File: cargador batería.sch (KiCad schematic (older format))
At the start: 4 parts, among them U2 MCP73831-2-OT

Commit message: Esquema corregido, PCB terminada
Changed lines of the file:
@@
 EESchema Schematic File Version 4
+LIBS:tpFinal-cache
 EELAYER 26 0
 EELAYER END
@@
 encoding utf-8
 Sheet 2 6
-Title ""
-Date ""
-Rev ""
-Comp ""
+Title "Sistema de comunicación en tiempo real por mensajes de voz
+"
+Date "2018-10-16"
+Rev "1.0"
+Comp "Marcelo Pistarelli"
 Comment1 ""
 Comment2 ""
@@
 Wire Wire Line
 	4750 3600 4900 3600
-Wire Wire Line
-	5300 3800 5300 3950
-Wire Wire Line
-	4750 3950 5300 3950
-Connection ~ 5300 3950
 $Comp
 L Device:C C?
@@
 	1    0    0    -1
 $EndComp
-Wire Wire Line
-	4300 3950 4750 3950
-Connection ~ 4750 3950
 $Comp
 L Device:C C?
@@
 $EndComp
 Wire Wire Line
-	4300 3650 4300 3950
-Wire Wire Line
 	4300 3350 4300 3200
 Wire Wire Line
@@
 Wire Wire Line
 	6400 3400 6400 3450
-Wire Wire Line
-	6400 3750 6400 3950
-Wire Wire Line
-	6400 3950 5300 3950
 Text HLabel 6800 3400 2    50   Output ~ 0
 BAT+
@@
 	6800 3400 6400 3400
 Connection ~ 6400 3400
-Text HLabel 6800 3950 2    50   Output ~ 0
+Text HLabel 6800 4000 2    50   Output ~ 0
 BAT-
-Wire Wire Line
-	6800 3950 6400 3950
-Connection ~ 6400 3950
 Text HLabel 6800 3150 2    50   Output ~ 0
 CHGR_STAT
@@
 Wire Wire Line
 	6100 3150 6800 3150
-Text HLabel 4000 3950 0    50   Input ~ 0
+Text HLabel 4000 4000 0    50   Input ~ 0
 GND
-Wire Wire Line
-	4000 3950 4300 3950
-Connection ~ 4300 3950
 Text HLabel 4000 3200 0    50   Input ~ 0
 V+
@@
 	4000 3200 4300 3200
 Connection ~ 4300 3200
+Wire Wire Line
+	4000 4000 4300 4000
+Wire Wire Line
+	4750 3950 4750 4000
+Connection ~ 4750 4000
+Wire Wire Line
+	4750 4000 5300 4000
+Wire Wire Line
+	4300 3650 4300 4000
+Connection ~ 4300 4000
+Wire Wire Line
+	4300 4000 4750 4000
+Wire Wire Line
+	5300 3800 5300 4000
+Connection ~ 5300 4000
+Wire Wire Line
+	5300 4000 6400 4000
+Wire Wire Line
+	6400 3750 6400 4000
+Connection ~ 6400 4000
+Wire Wire Line
+	6400 4000 6800 4000
 $EndSCHEMATC

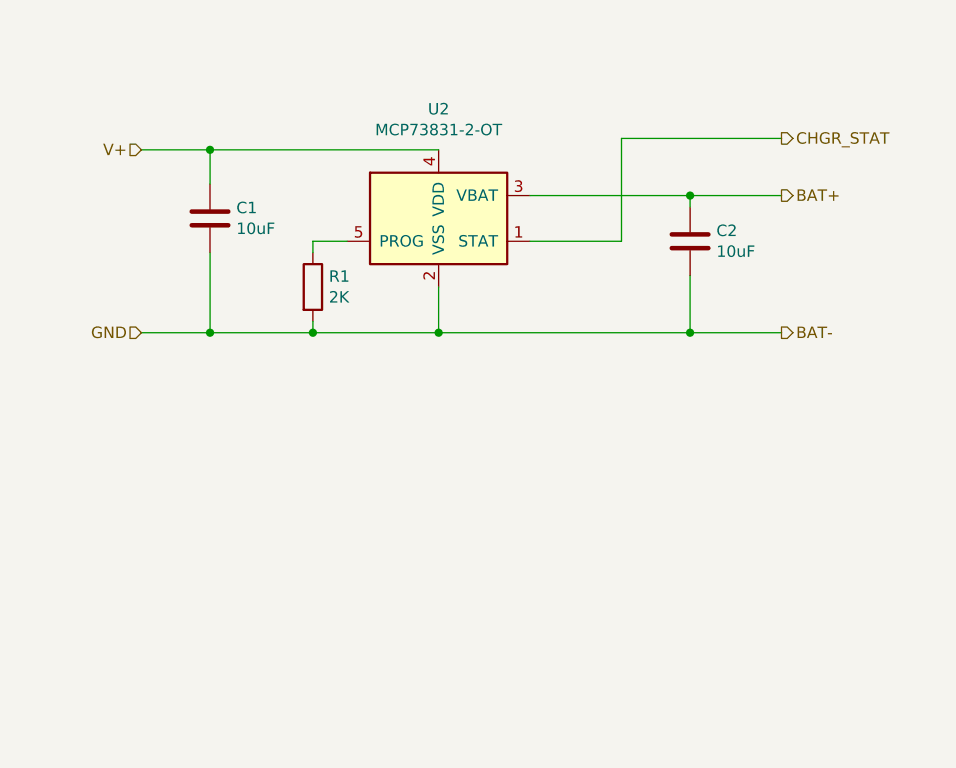
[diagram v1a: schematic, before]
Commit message: Se aplicaron correciones indicadas por el profesor en el esquemático
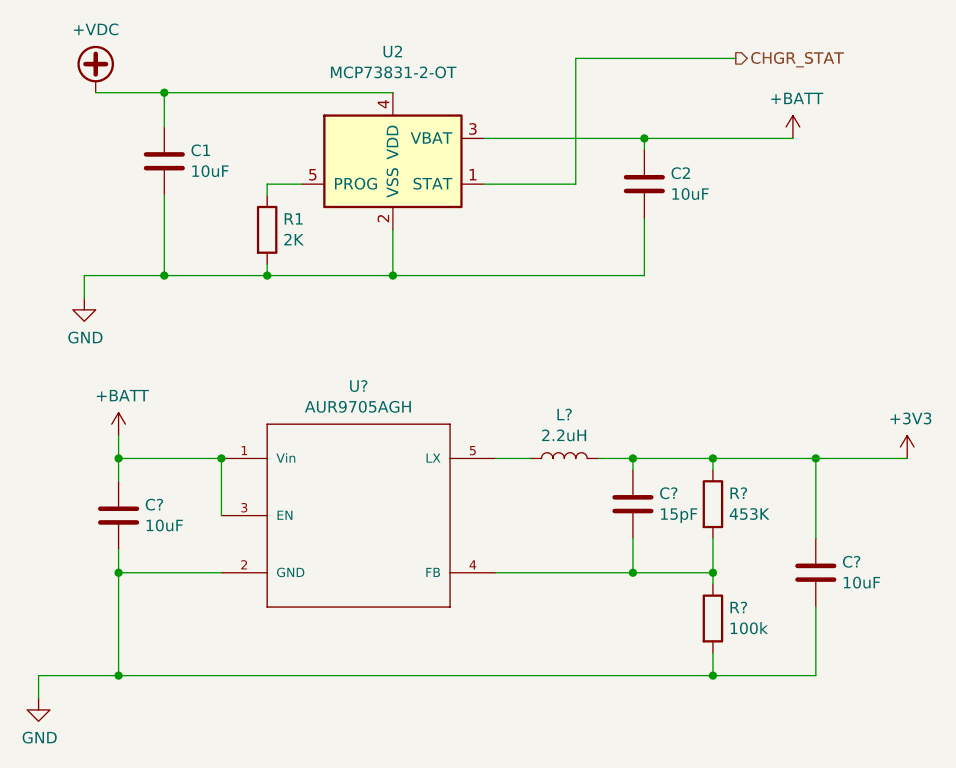
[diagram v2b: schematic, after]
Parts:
- added C? (x2): 10uF, Capacitor_SMD:C_0805_2012Metric, symbol Device:C
- added C?: 15pF, Capacitor_SMD:C_0805_2012Metric, symbol Device:C
- added L?: 2.2uH, Inductor_SMD:L_1210_3225Metric, symbol Device:L
- added R?: 453K, Resistor_SMD:R_0805_2012Metric, symbol Device:R
- added R?: 100k, Resistor_SMD:R_0805_2012Metric, symbol Device:R
- added U?: AUR9705AGH, Package_TO_SOT_SMD:SOT-23-5, symbol tpfinal:AUR9705AGH
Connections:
- net BAT+ renamed +BATT
- net +BATT: now also C?.1, U?.1 (Vin), U?.3 (EN)
- net BAT- renamed GND
- net GND: now also C?.2, C?.2, R?.2, U?.2 (GND)
- net V+ renamed +VDC
- new net: C?.2, R?.1, R?.2, U?.4 (FB)
- new net: L?.1, U?.5 (LX)
- new net +3V3: C?.1, C?.1, L?.2, R?.1
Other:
- moved on the sheet: C1, C2, R1, U2
